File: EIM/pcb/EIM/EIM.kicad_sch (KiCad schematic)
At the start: 26 parts, among them J1 MX34028NF2, J2 36783-1201, J3 34830-0801, J4 34830-2001, J7 DEBUG1, J8 DEBUG2, K1 G8N-1L-AS_DC12

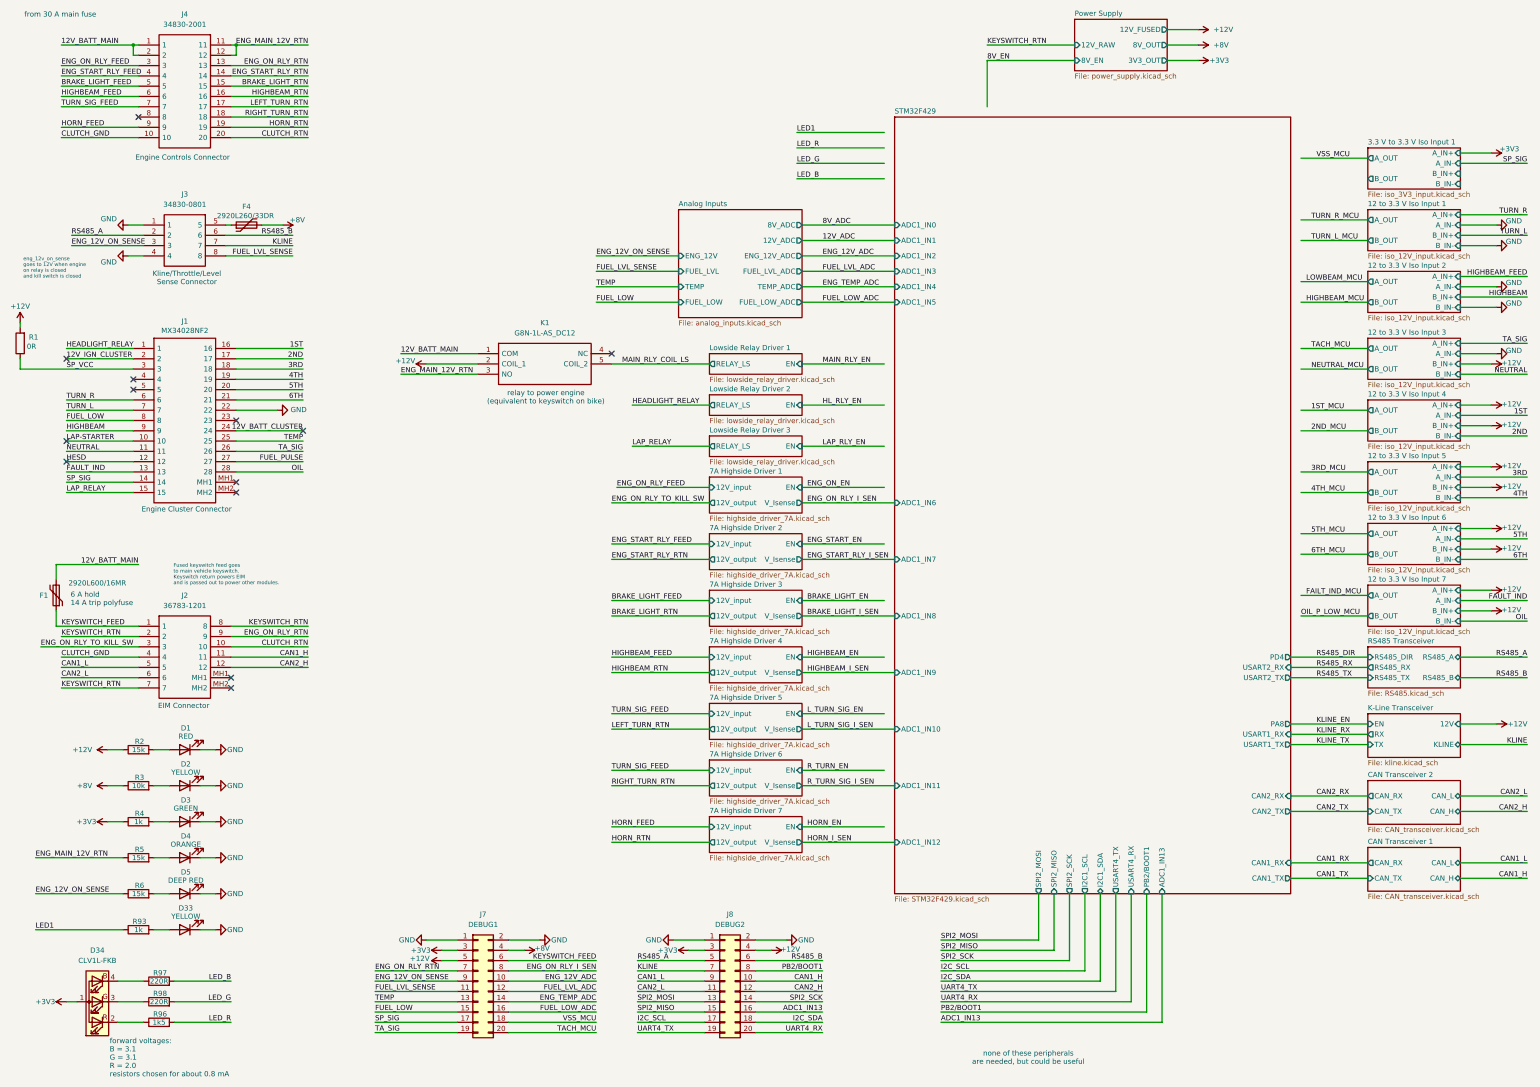
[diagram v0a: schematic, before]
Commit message: Layout 75% done, before 8V bus deletion
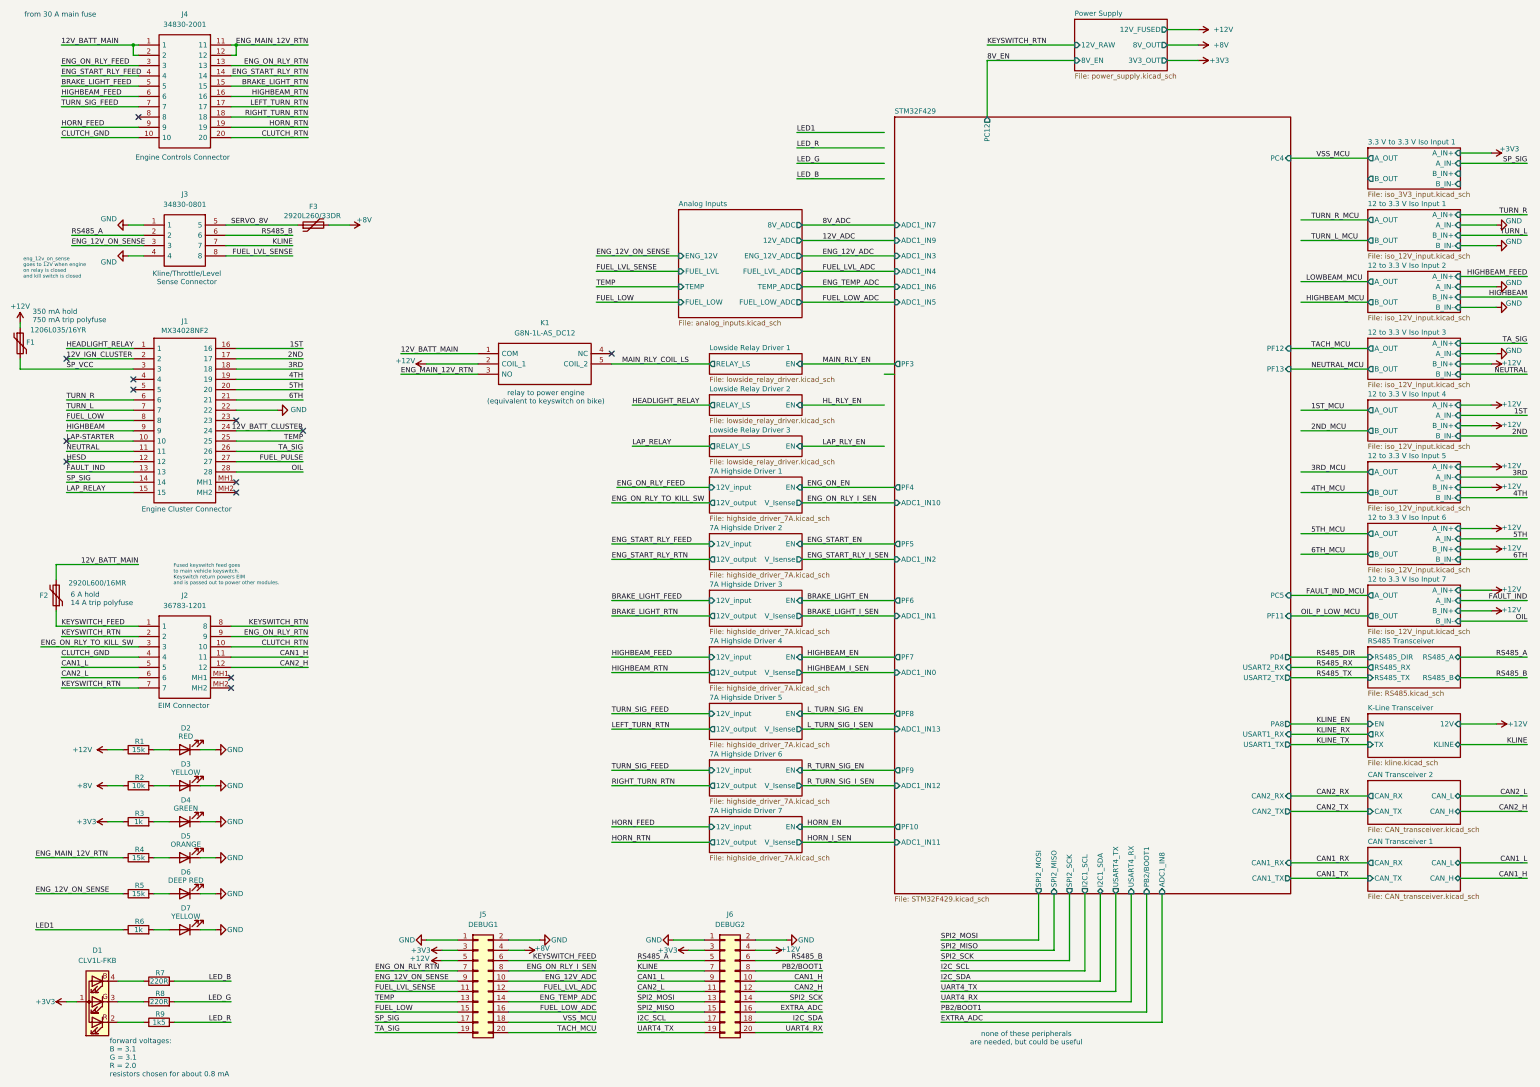
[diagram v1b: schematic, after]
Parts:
- removed R1: 0R, Resistor_SMD:R_0805_2012Metric_Pad1.20x1.40mm_HandSolder, symbol Device:R
- added F1: 1206L035/16YR, Fuse:Fuse_1206_3216Metric, symbol Device:Polyfuse
- renumbered D34 to D1, D1 to D2, D2 to D3, D3 to D4, D4 to D5, D5 to D6, D33 to D7, F1 to F2, F4 to F3, J7 to J5, J8 to J6, R2 to R1, R3 to R2, R4 to R3, R5 to R4, R6 to R5, R93 to R6, R97 to R7, R98 to R8, R96 to R9
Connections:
- net +12V: now also F1.1
- net SP_VCC: now also F1.2
- net SERVO_8V: now reaches F3.1, J3.5
- net ADC1_IN13 renamed EXTRA_ADC
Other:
- sheet STM32F429 ports: added PC12, PC4, PC5, PF10, PF11, PF12, PF13, PF3, PF4, PF5, PF6, PF7, PF8, PF9; removed none
- note added: "350 mA hold 750 mA trip polyfuse"
- moved on the sheet: F3

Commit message: All components placed and pins assigned.
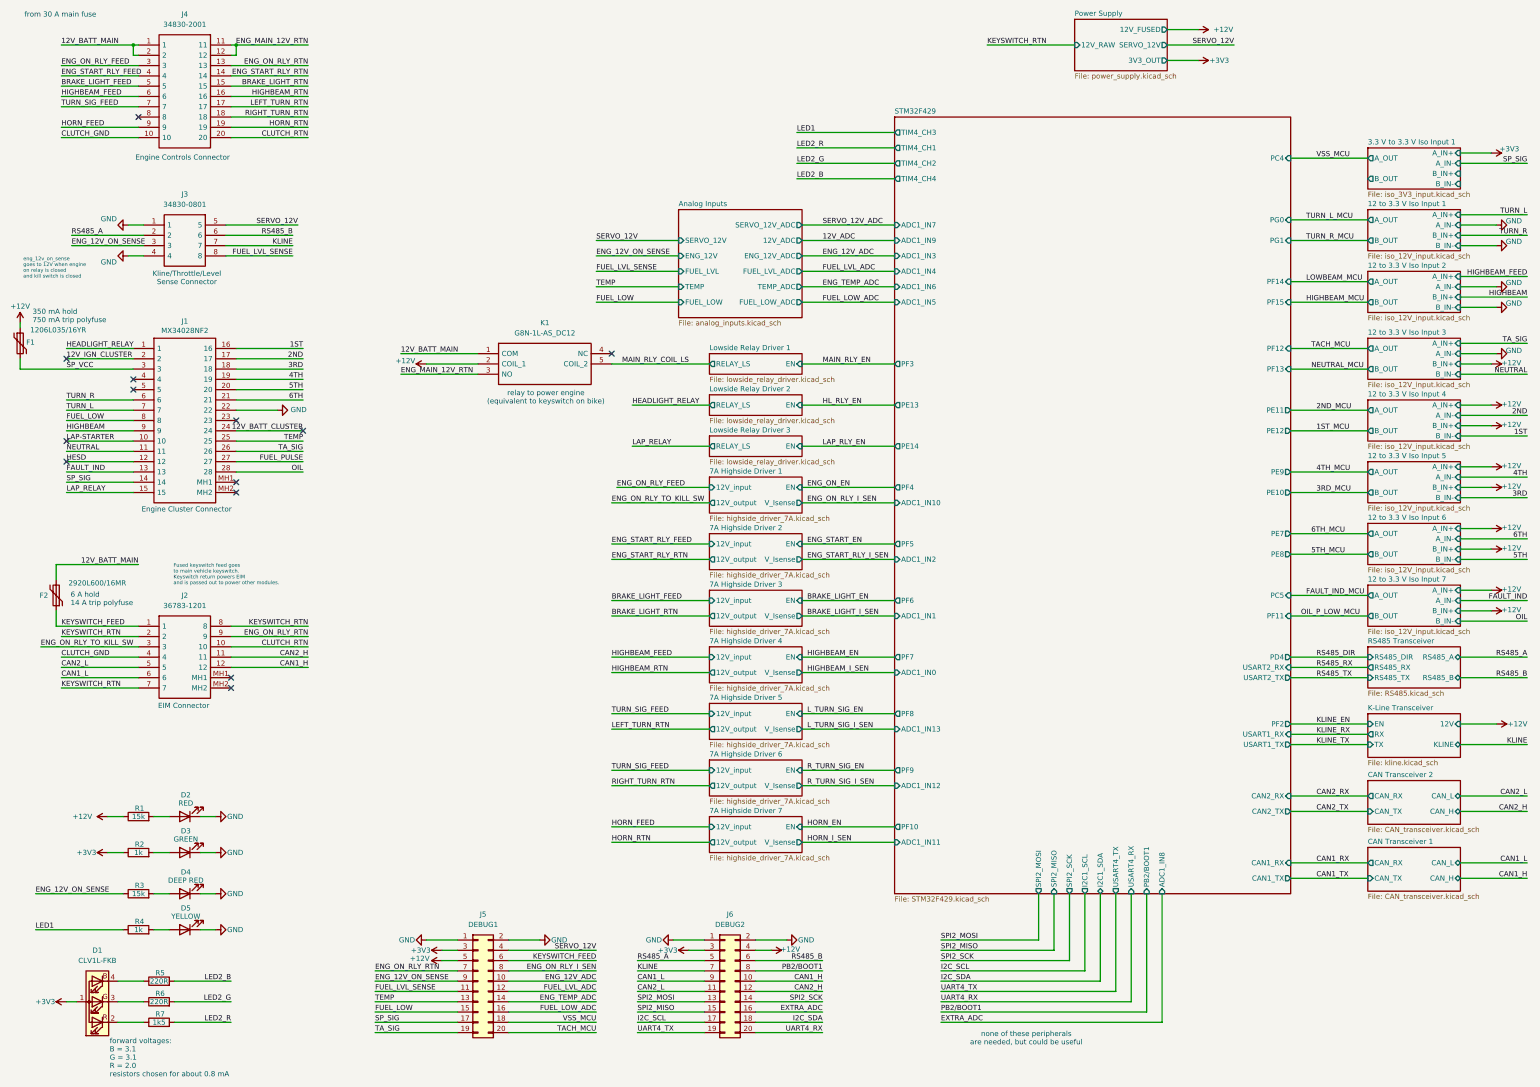
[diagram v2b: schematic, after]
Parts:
- removed D3: YELLOW, LED_SMD:LED_0805_2012Metric, symbol Device:LED
- removed D5: ORANGE, LED_SMD:LED_0805_2012Metric, symbol Device:LED
- removed F3: 2920L260/33DR, Fuse:Fuse_2920_7451Metric, symbol Device:Polyfuse
- removed R2: 10k, Resistor_SMD:R_0805_2012Metric_Pad1.20x1.40mm_HandSolder, symbol Device:R
- removed R4: 15k, Resistor_SMD:R_0805_2012Metric_Pad1.20x1.40mm_HandSolder, symbol Device:R
- renumbered D4 to D3, D6 to D4, D7 to D5, R3 to R2, R5 to R3, R6 to R4, R7 to R5, R8 to R6, R9 to R7
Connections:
- net SERVO_8V is gone; now on net SERVO_12V: J3.5
- net CAN1_H: now also J2.12; no longer J2.11
- net CAN1_L: now also J2.6; no longer J2.5
- net CAN2_H: now also J2.11; no longer J2.12
- net CAN2_L: now also J2.5; no longer J2.6
- net +8V renamed SERVO_12V
- net LED_B renamed LED2_B
- net LED_G renamed LED2_G
- net LED_R renamed LED2_R
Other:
- sheet Analog Inputs ports: added SERVO_12V, SERVO_12V_ADC; removed 8V_ADC
- sheet Power Supply ports: added SERVO_12V; removed 8V_EN, 8V_OUT
- sheet STM32F429 ports: added PE10, PE11, PE12, PE13, PE14, PE7, PE8, PE9, PF14, PF15, PF2, PG0, PG1, TIM4_CH1, TIM4_CH2, TIM4_CH3, TIM4_CH4; removed PA8, PC12
- moved on the sheet: D2, D3, R1, R2
